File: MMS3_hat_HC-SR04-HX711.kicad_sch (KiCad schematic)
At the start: 15 parts, among them J4 Debug_USART_TX, U3 AMS1117

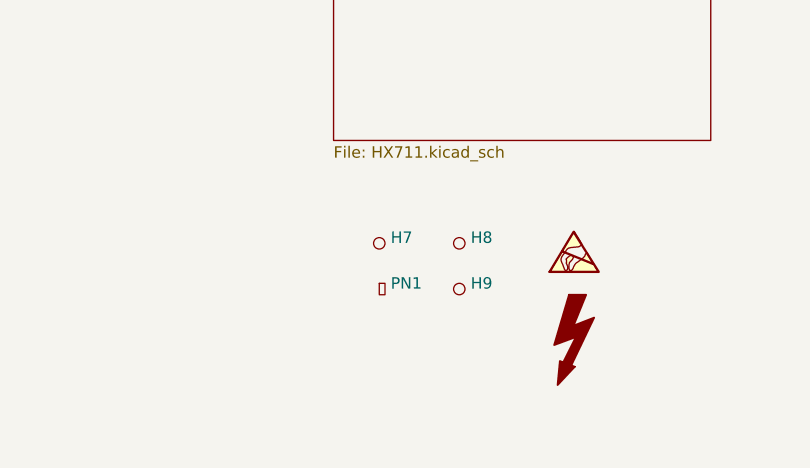
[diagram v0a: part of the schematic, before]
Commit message: updated bus switch to sensible one
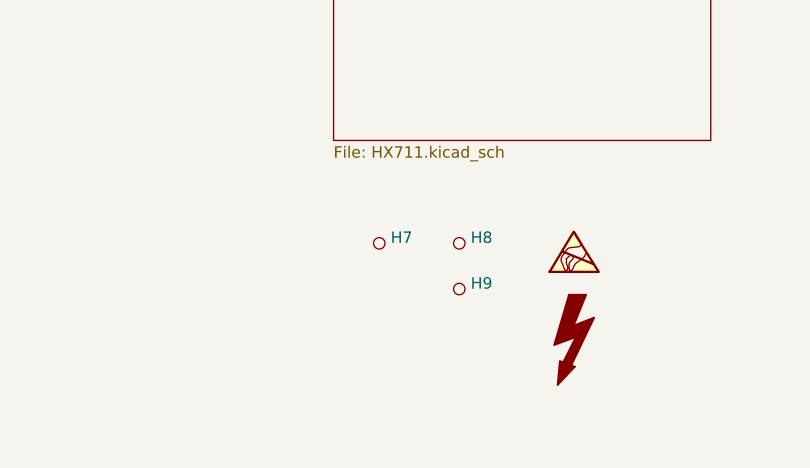
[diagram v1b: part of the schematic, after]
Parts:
- removed PN1: ~, PCM_JLCPCB:Part_Num_JLCPCB, symbol PCM_JLCPCB-Manufacturing:Part Number, PCM_JLCPCB, 0.8x0.15mm
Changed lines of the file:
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@@
-	)
-	(symbol
-		(lib_id "PCM_JLCPCB-Manufacturing:Part Number, PCM_JLCPCB, 0.8x0.15mm")
-		(at 140.97 173.99 0)
-		(unit 1)
-		(exclude_from_sim no)
-		(in_bom yes)
-		(on_board yes)
-		(dnp no)
-		(fields_autoplaced yes)
-		(property "Reference" "PN1"
-			(at 142.24 173.3549 0)
-			(effects
-				(font
-					(size 1.27 1.27)
-				)
-				(justify left)
-			)
-		)
-		(property "Value" "~"
-			(at 142.24 175.26 0)
-			(effects
-				(font
-					(size 1.27 1.27)
-				)
-				(justify left)
-			)
-		)
-		(property "Footprint" "PCM_JLCPCB:Part_Num_JLCPCB"
-			(at 140.97 173.99 0)
-			(effects
-				(font
-					(size 1.27 1.27)
-				)
-				(hide yes)
-			)
-		)
-		(property "Datasheet" "https://jlcpcb.com/help/article/How-to-remove-order-number-from-your-PCB"
-			(at 140.97 173.99 0)
-			(effects
-				(font
-					(size 1.27 1.27)
-				)
-				(hide yes)
-			)
-		)
-		(property "Description" "To indicate the location, simply add the text \"JLCJLCJLCJLC\" to the silk layer and select the \"Specify a location\" option when placing your order. Please note that if this option is not chosen, we may not notice that you have added the text.   Note: Use only \"JLCJLCJLCJLC\" without any additional characters. The font size should be larger than 0.8mm in height and 0.15mm in width."
-			(at 140.97 173.99 0)
-			(effects
-				(font
-					(size 1.27 1.27)
-				)
-				(hide yes)
-			)
-		)
-		(property "Sim.Device" ""
-			(at 140.97 173.99 0)
-			(effects
-				(font
-					(size 1.27 1.27)
-				)
-				(hide yes)
-			)
-		)
-		(instances
-			(project "MMS3_hat_templates"
-				(path "/6596548a-44e0-46d8-8624-fd71cf4a3e17"
-					(reference "PN1")
-					(unit 1)
-				)
-			)
-		)
 	)
 	(symbol
